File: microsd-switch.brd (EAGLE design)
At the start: 49.2 x 41.9 mm, 12 parts, among them IC1 SN74CBT3257D, IC2 SN74CBT3257D, U1 USD-SOCKETNEW

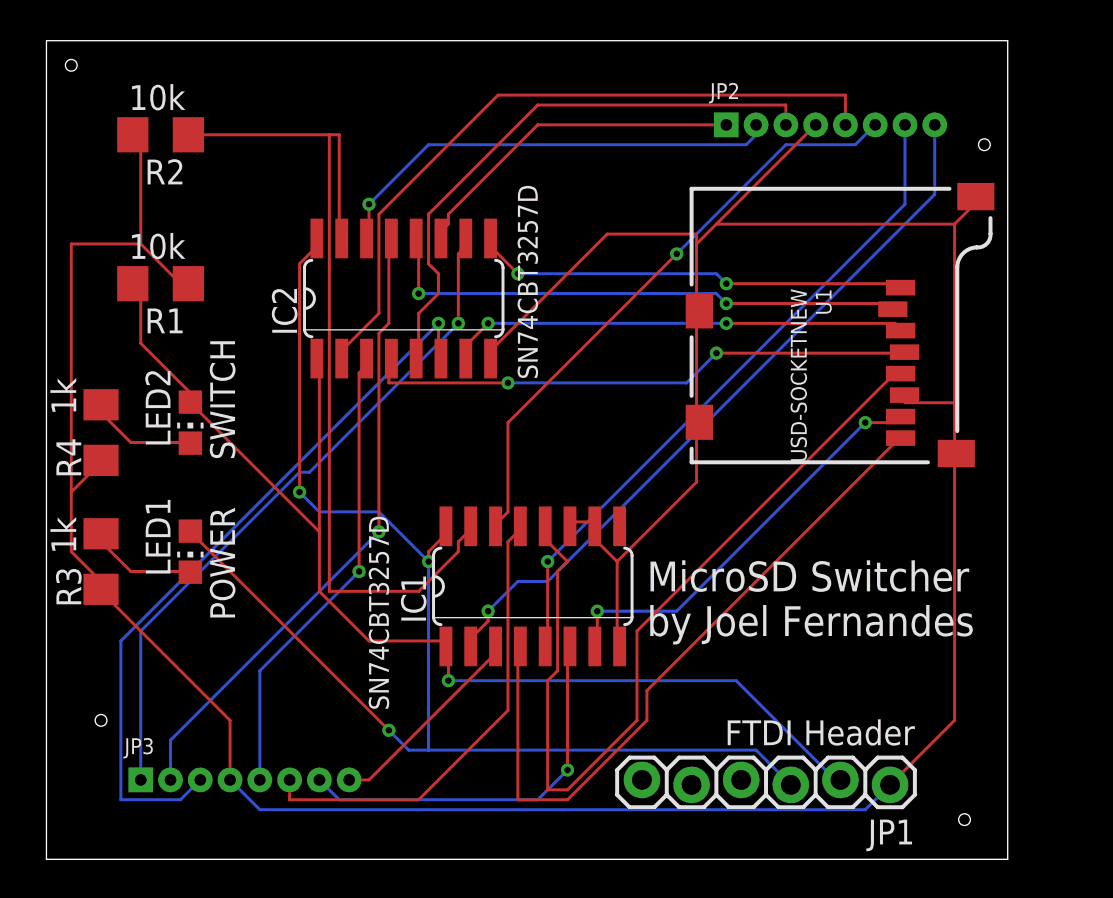
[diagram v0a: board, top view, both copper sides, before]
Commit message: Revert "Reduced uSD header connector size."
This reverts commit 164ab6429ac06b889099512f0f315f421e6ea5d6.
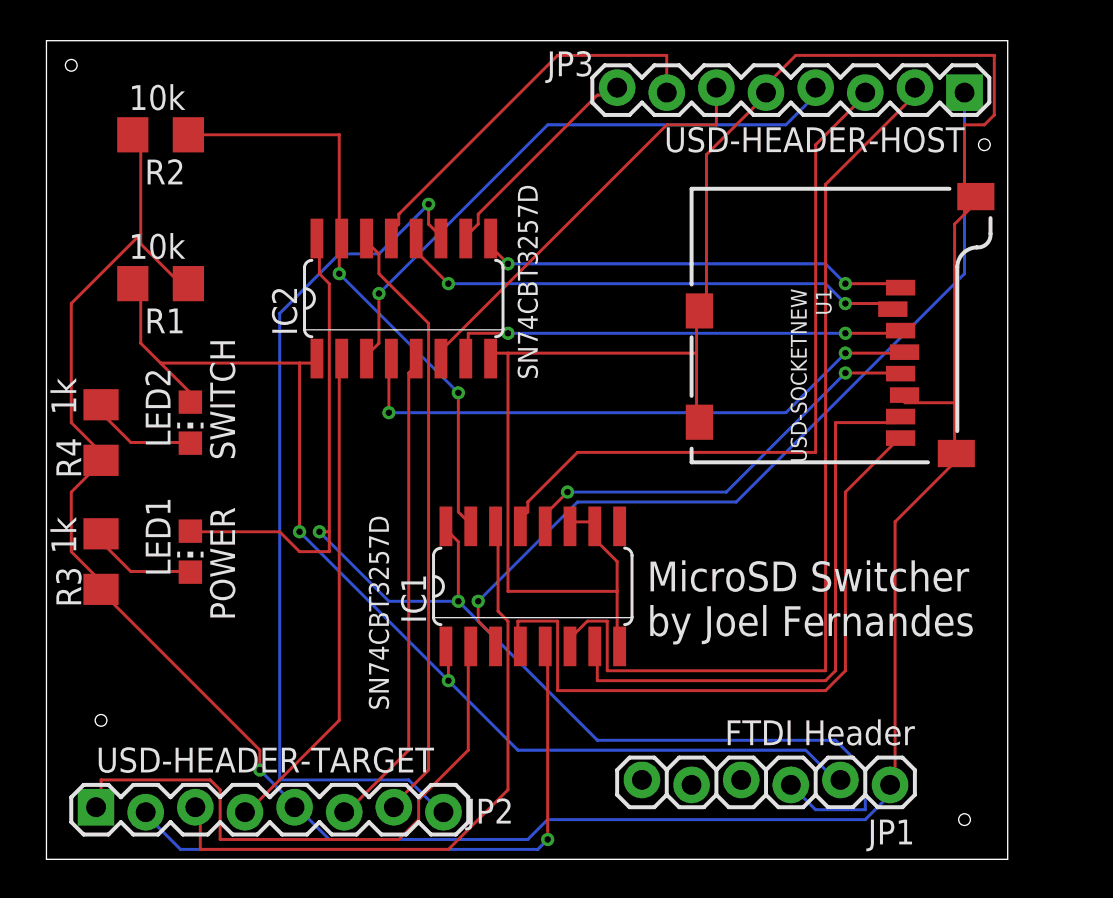
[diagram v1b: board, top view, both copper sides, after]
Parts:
- JP2: value SD_HEADER_TARGET -> USD-HEADER-TARGET; device joels-parts:1X08_SMALL -> SparkFun:1X08_LOCK
- JP3: value SD_HEADER_HOST -> USD-HEADER-HOST; device joels-parts:1X08_SMALL -> SparkFun:1X08_LOCK
- moved JP2 51.2 mm to (36.8, 40.6)
- moved JP3 51.2 mm to (81.3, 77.5), turned to 180 degrees
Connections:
- net CLK-A: now also JP2.3; no longer JP2.6
- net CLK-B: now also JP3.3; no longer JP3.6
- net CMD-A: now also JP2.6; no longer JP2.3
- net CMD-B: now also JP3.6; no longer JP3.3
- net DAT0-A: now also JP2.2; no longer JP2.7
- net DAT0-B: now also JP3.2; no longer JP3.7
- net DAT1-A: now also JP2.1; no longer JP2.8
- net DAT1-B: now also JP3.1; no longer JP3.8
- net DAT2-A: now also JP2.8; no longer JP2.1
- net DAT2-B: now also JP3.8; no longer JP3.1
- net DAT3-A: now also JP2.7; no longer JP2.2
- net DAT3-B: now also JP3.7; no longer JP3.2
- net GND: now also JP2.5, JP3.5; no longer JP2.4, JP3.4
- net VDD-A: now also JP2.4; no longer JP2.5
- net VDD-B: now also JP3.4; no longer JP3.5
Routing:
- net DAT1-B: track 10.6 -> 43.9 mm, vias 0 -> 1
- net DAT0-B: track 20.1 -> 48.2 mm, vias 1 -> 0
- net DAT2-A: track 17.6 -> 44.8 mm, vias 0 -> 1
- net DAT2-B: track 35.0 -> 11.5 mm, vias 1 -> 0
- net N$1: track 43.9 -> 21.8 mm, vias 0 -> 2
- net CMD-B: track 37.4 -> 21.3 mm, vias 1 -> 0
- net OE: track 45.4 -> 30.6 mm, vias 0 -> 2
- net GND: track 177.4 -> 191.6 mm, vias 0 -> 1
- net CLK-B: track 23.7 -> 36.7 mm
- net DAT3-B: track 32.4 -> 20.5 mm, vias 1 -> 0
- net VDD-A: track 36.2 -> 25.3 mm
- net DAT0-Y: track 21.5 -> 30.4 mm, vias 2 -> 0
- net DAT3-A: track 23.6 -> 31.1 mm, vias 1 -> 0
- net DAT1-A: track 37.5 -> 30.9 mm, vias 1 -> 0
- net VDD-B: track 23.9 -> 30.5 mm
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
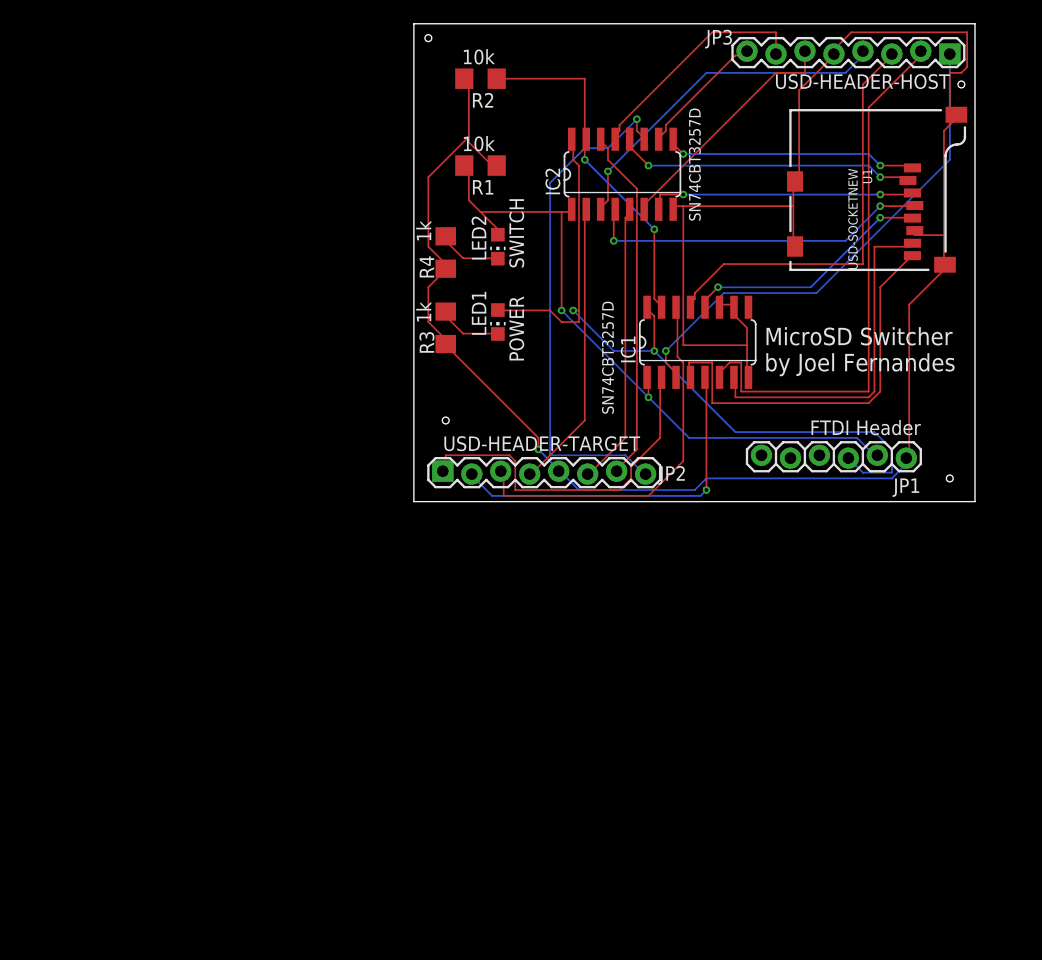
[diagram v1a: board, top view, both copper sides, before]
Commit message: microsd-switch: Update board/schematic
Signed-off-by: Joel Fernandes <joelf@ti.com>
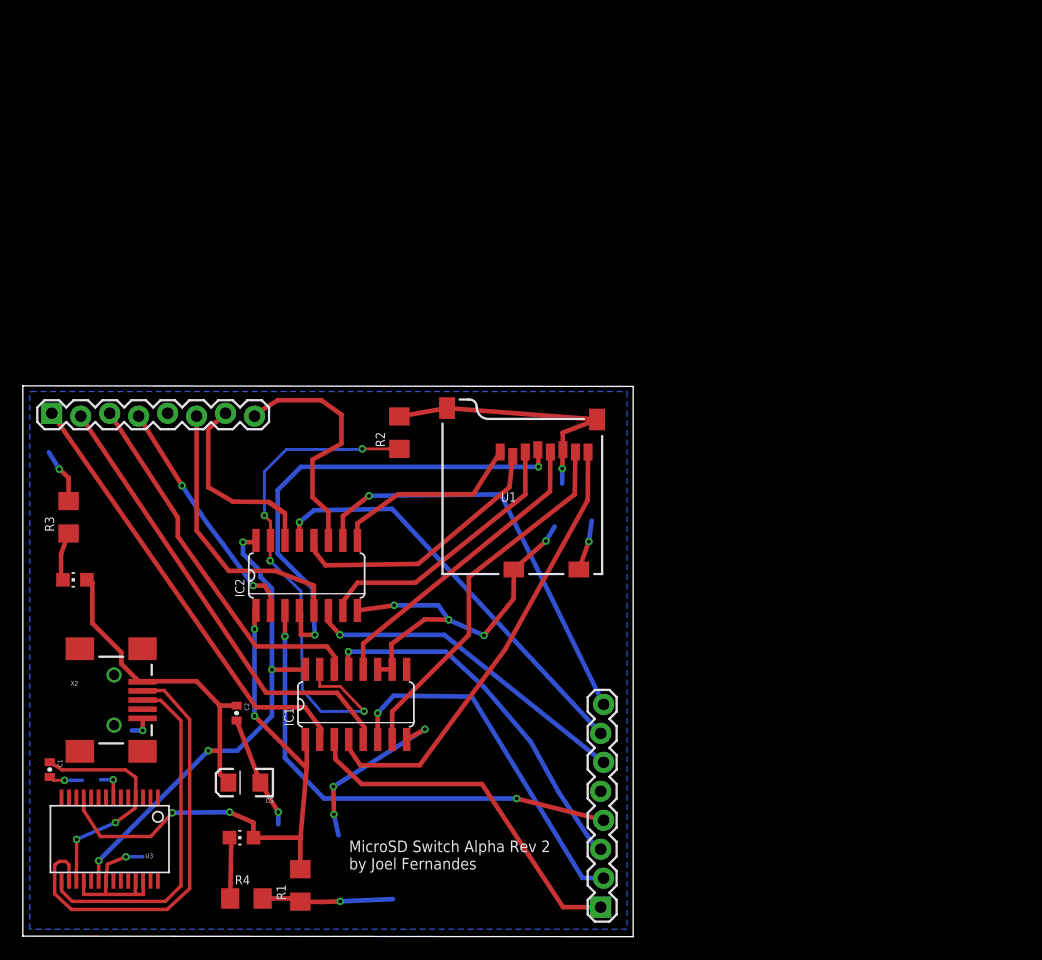
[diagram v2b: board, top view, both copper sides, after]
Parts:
- removed JP1: FTDI Header, SparkFun:1X06_LOCK
- added C1, C2: 0.1uF, SparkFun:0402-CAP
- added C5: 10uF, SparkFun:EIA3216
- added U3: FT232RLSSOP, SparkFun:SSOP28DB
- added X2: USB-SMD-NS, SparkFun:USB-MINIB-NOSTOP
- moved JP3 80.9 mm to (50.8, 2.54), turned to 90 degrees
- moved R1 65.1 mm to (24.3, 4.45), turned to 90 degrees
- moved R4 59.3 mm to (19.6, 3.30), turned to 0 degrees
- moved LED2 56.5 mm to (19.2, 8.64), turned to 90 degrees
- moved IC2 44.8 mm to (24.9, 31.6)
- moved IC1 43.7 mm to (29.2, 20.3)
- moved LED1 43.4 mm to (4.57, 31.2), turned to 90 degrees
- moved R3 37.0 mm to (4.01, 36.7), turned to 90 degrees
- moved JP2 34.7 mm to (2.54, 45.7)
- moved R2 31.8 mm to (33.0, 44.1), turned to 90 degrees
- moved U1 31.4 mm to (50.8, 31.8), turned to 0 degrees
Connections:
- net N$1 renamed CLK-Y
- new net 3.3V: C1.1, U3.17, U3.4
- new net USB_D+: U3.15, X2.D+
- new net USB_D-: U3.16, X2.D-
- net GND: now also C1.2, C2.2, C5.C, U3.18, U3.21, U3.25, U3.26, U3.7, X2.GND; no longer JP1.1
- net HOSTSELECT: now also U3.11; no longer JP1.2
- net VCC: now also C2.1, C5.A, U3.20, X2.VBUS; no longer JP1.3
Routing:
- net GND: track 191.6 -> 127.5 mm, vias 1 -> 16
- net USB_D-: track 0.00 -> 38.6 mm
- net USB_D+: track 0.00 -> 30.9 mm
- net DAT2-B: track 11.5 -> 37.1 mm, vias 0 -> 1
- net DAT2-A: track 44.8 -> 21.7 mm, vias 1 -> 0
- net 3.3V: track 0.00 -> 20.1 mm, vias 0 -> 2
- net DAT0-B: track 48.2 -> 31.7 mm, vias 0 -> 1
- net DAT3-B: track 20.5 -> 37.0 mm, vias 0 -> 1
- net OE: track 30.6 -> 45.8 mm, vias 2 -> 4
- net DAT3-A: track 31.1 -> 18.4 mm
- net DAT1-B: track 43.9 -> 31.7 mm, vias 1 -> 0
- net N$2: track 30.5 -> 42.6 mm
- net VDD-B: track 30.5 -> 42.6 mm, vias 1 -> 2
- net DAT0-A: track 31.5 -> 40.4 mm, vias 1 -> 0
- net CMD-B: track 21.3 -> 29.6 mm, vias 0 -> 1
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- added copper zone on layer 16, net GND
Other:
- board size 49.2 x 41.9 mm -> 53.5 x 48.3 mm
- board text added: "MicroSD Switch Alpha Rev 2 by Joel Fernandes"
- board text removed: "MicroSD Switcher by Joel Fernandes"
